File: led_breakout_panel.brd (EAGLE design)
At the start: 48.9 x 21 mm, 40 parts

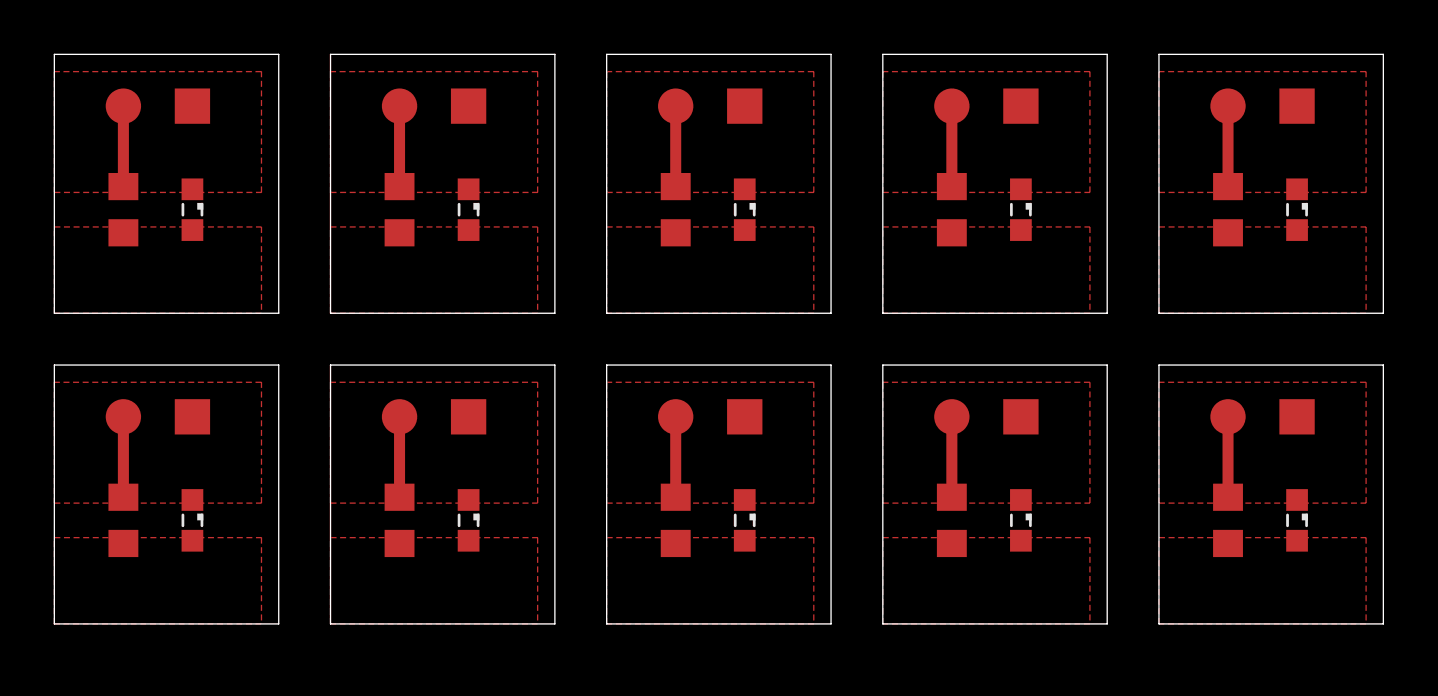
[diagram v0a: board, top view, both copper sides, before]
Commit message: tighter panel
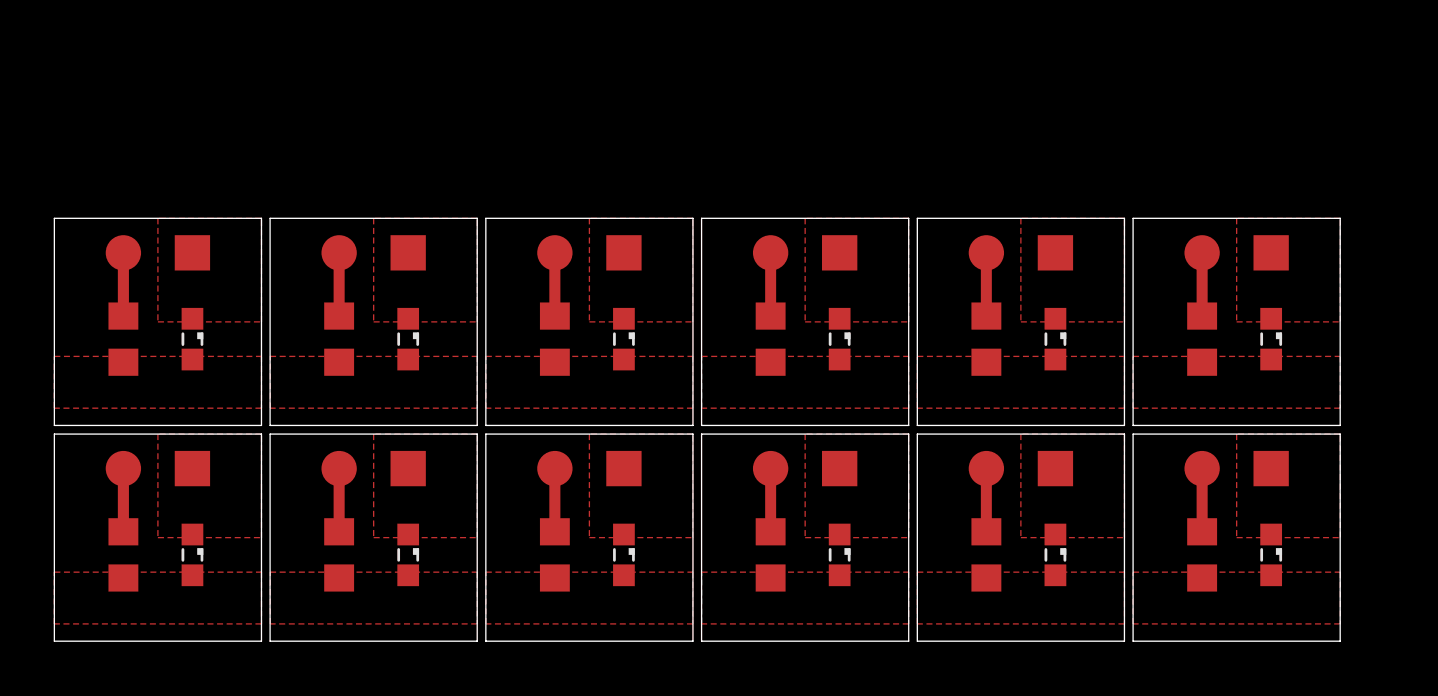
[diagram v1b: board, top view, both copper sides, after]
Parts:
- added 5V10, 5V11: TPTP13R, testpad:TP13R
- added GND10, GND11: TPTP13SQ, testpad:TP13SQ
- added LED11, LED12: (no value), led:SML0603
- added R11, R12: 220, rcl:R0603
- moved 5V8 16.0 mm to (34.3, 6.35)
- moved GND8 16.0 mm to (36.8, 6.35)
- moved LED9 15.5 mm to (36.8, 3.17)
- moved R9 15.5 mm to (34.3, 3.17)
- moved 5V6 14.9 mm to (26.4, 6.35)
- moved GND6 14.9 mm to (28.9, 6.35)
- moved LED7 14.3 mm to (28.9, 3.17)
- moved R7 14.3 mm to (26.4, 3.17)
- moved 5V4 14.1 mm to (18.4, 6.35)
- moved GND4 14.1 mm to (21.0, 6.35)
- moved 5V2 13.5 mm to (10.5, 6.35)
- moved GND2 13.5 mm to (13.0, 6.35)
- moved LED5 13.5 mm to (21.0, 3.17)
- moved R5 13.5 mm to (18.4, 3.17)
- moved LED3 12.9 mm to (13.0, 3.17)
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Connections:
- new net 5V10: 5V10.TP, R11.1
- new net 5V11: 5V11.TP, R12.1
- new net GND10: GND10.TP, LED11.C
- new net GND11: GND11.TP, LED12.C
- new net LEDSUPPLY10: LED11.A, R11.2
- new net LEDSUPPLY11: LED12.A, R12.2
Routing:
- net 5V11: track 0.00 -> 2.32 mm
- net 5V10: track 0.00 -> 2.32 mm
- net 5V9: track 2.96 -> 2.32 mm
- net 5V7: track 2.96 -> 2.32 mm
- net 5V5: track 2.96 -> 2.32 mm
- net 5V3: track 2.96 -> 2.32 mm
- net 5V: track 2.96 -> 2.32 mm
- net 5V8: track 2.96 -> 2.32 mm
- net 5V6: track 2.96 -> 2.32 mm
- net 5V4: track 2.96 -> 2.32 mm
- net 5V2: track 2.96 -> 2.32 mm
- net 5V1: track 2.96 -> 2.32 mm
- added copper zone on layer 1, net GND10
- added copper zone on layer 1, net GND11
- added copper zone on layer 1, net LEDSUPPLY10
- added copper zone on layer 1, net LEDSUPPLY11
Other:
- board size 48.9 x 21 mm -> 47.3 x 15.6 mm
